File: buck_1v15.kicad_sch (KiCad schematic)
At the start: 21 parts

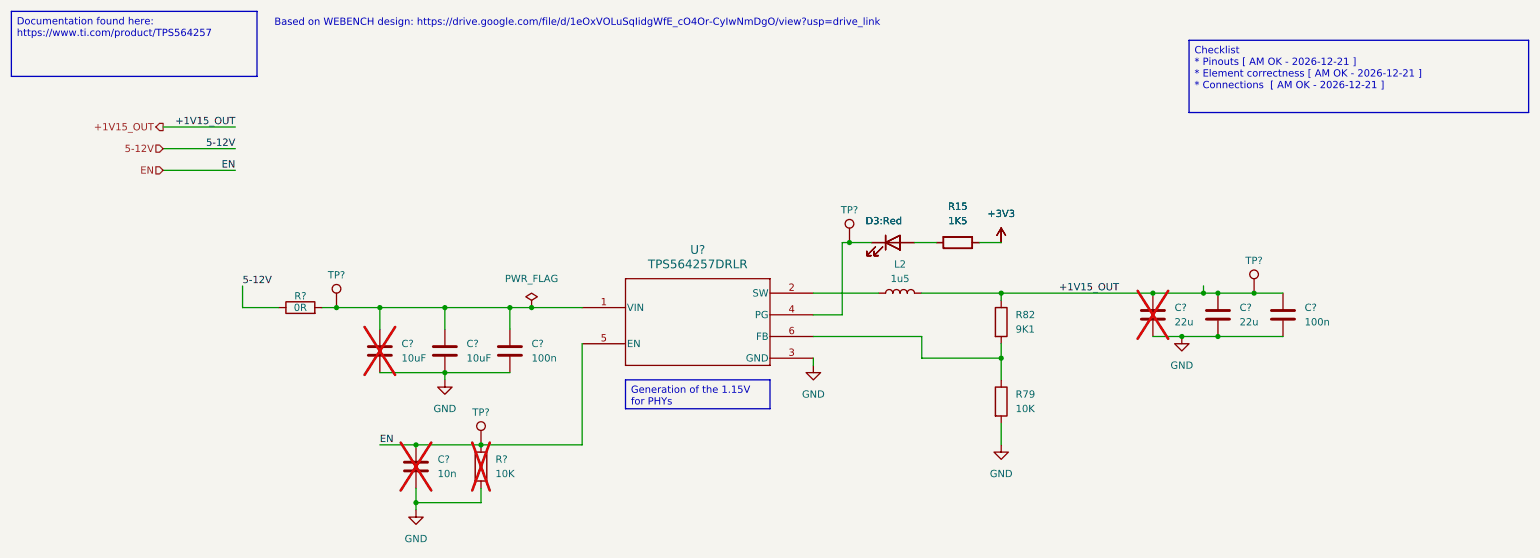
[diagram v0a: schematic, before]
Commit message: towards a merge conflict free schematic. Refs: #9
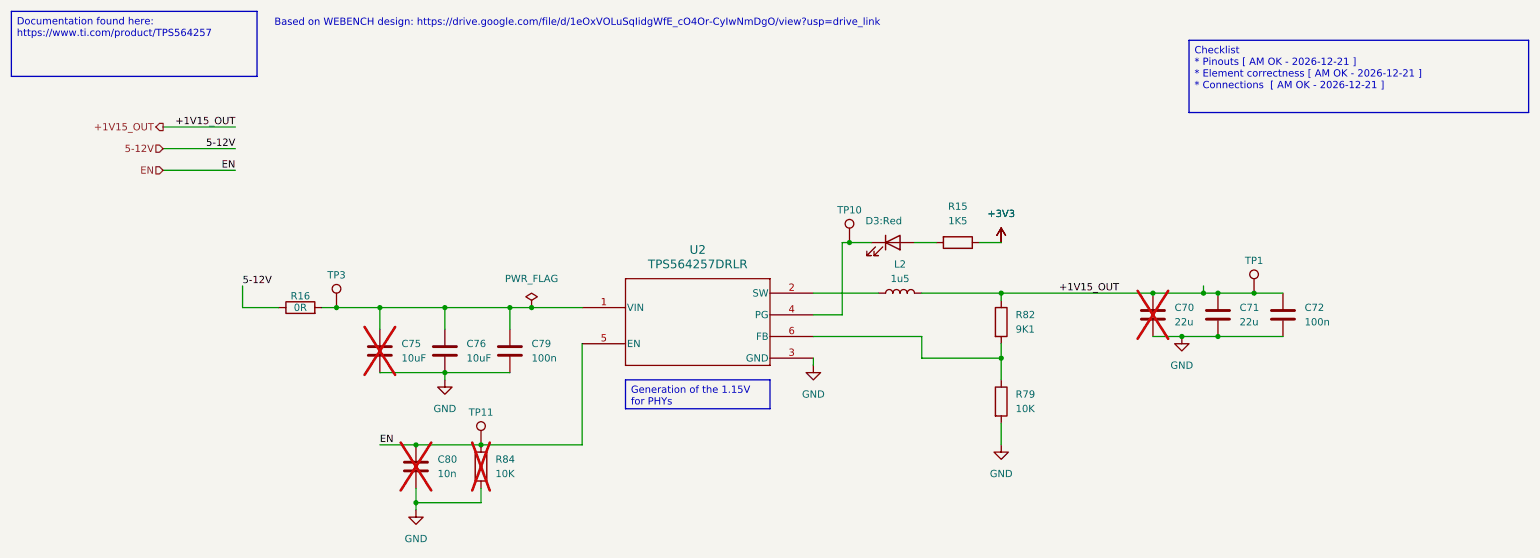
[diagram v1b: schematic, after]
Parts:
- removed D3: LED_{color}_{U_F}_{I_F}, KL_Footprints:LED_0603, symbol KL_LED:LED_red_2V_0.03A
- removed R15: 1K5, KL_Footprints:R_0603, symbol KL_R:R_1K5_100mW_5_0603
- gave numbers to parts that had none: 14

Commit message: open project in KiCAD10. Refs: #41
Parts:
- TP1, TP10, TP11, TP3: value ~ -> (none)

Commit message: updates buck_1v15. Refs: #41
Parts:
- removed C72: 100n, KL_Footprints:C_0603, symbol KL_C:C_100n_10V_X7R_0603_10
- added C72: 100n, KL_Footprints:C_0603, symbol KL_C:C_100n_16V_10pct_X7R_0603
- C70, C71: symbol KL_C:C_22u_10V_X5R_0603_20 -> KL_C:C_22u_10V_20pct_X5R_0603; Dielectric (none) -> X5R; MPN (none) -> GRM187R61A226ME15D; Package_in_inch (none) -> 0603; Tolerance 20 -> (none); Tolerance_in_pct (none) -> 20; Voltage 10V -> (none); Voltage_in_V (none) -> 10
- C75, C76: value 10uF -> 10u; symbol KL_C:C_10u_25V_X5R_0603_20 -> KL_C:C_10u_25V_20pct_X5R_0603; Dielectric (none) -> X5R; MPN (none) -> CL10A106MA8NRNC; Package_in_inch (none) -> 0603; Tolerance 20 -> (none); Tolerance_in_pct (none) -> 20; Voltage 25 -> (none); Voltage_in_V (none) -> 25
- C79: symbol KL_C:C_100n_16V_X7R_0603_10 -> KL_C:C_100n_16V_10pct_X7R_0603; Dielectric (none) -> X7R; MPN (none) -> CC0603KPX7R7BB104; Package_in_inch (none) -> 0603; Tolerance 10 -> (none); Tolerance_in_pct (none) -> 10; Voltage 16V -> (none); Voltage_in_V (none) -> 16
- C80: symbol KL_C:C_10n_50V_X7R_0603_10 -> KL_C:C_10n_50V_10pct_X7R_0603; Dielectric (none) -> X7R; MPN (none) -> CL10B103KB8WPND; Package_in_inch (none) -> 0603; Tolerance 10 -> (none); Tolerance_in_pct (none) -> 10; Voltage 50 -> (none); Voltage_in_V (none) -> 50
- D3: symbol KL_LED:LED_red_2V_0.03A -> KL_LED:LED_Red_2V_0.03A_0603; MPN (none) -> LTST-C194KRKT; Package_in_inch (none) -> 0603
- L2: symbol KL_L:L_1u5_19A_20pct_7L9x7W3 -> KL_L:L_1u5_19A_20pct_7.9x7.3; LCSC C2453564 -> C19947700; MPN (none) -> SRP7050WA-1R5M; Package_LxW_in_mm (none) -> 7.9x7.3; Package_in_inch 0L287X0W287 -> (none); Package_in_mm L7.9XW7.3 -> (none)
- R15: symbol KL_R:R_1K5_100mW_5_0603 -> KL_R:R_1K5_0.1W_5pct_0603; MPN (none) -> AC0603JR-071K5L; Package (in) 0603 -> (none); Package_in_inch (none) -> 0603; Power 0.1 -> (none); Power_in_W (none) -> 0.1; Tolerance 5 -> (none); Tolerance_in_pct (none) -> 5
- R16: symbol KL_R:R_0R_2W_5_2512 -> KL_R:R_0R_2W_5pct_2512; MPN (none) -> CRF2512-J/-000ELF; Mouser 652-CRF2512-J-000ELF -> 652-CRF2512-J-000ELF; Package (in) 2512 -> (none); Package_in_inch (none) -> 2512; Power 2 -> (none); Power_in_W (none) -> 2; Tolerance 5 -> (none); Tolerance_in_pct (none) -> 5
- R79, R84: symbol KL_R:R_10K_100mW_5_0603 -> KL_R:R_10K_0.1W_5pct_0603; MPN (none) -> CRCW060310K0JNEC; Package (in) 0603 -> (none); Package_in_inch (none) -> 0603; Power 100mW -> (none); Power_in_W (none) -> 0.1; Tolerance 5% -> (none); Tolerance_in_pct (none) -> 5
- R82: symbol KL_R:R_9K1_100mW_1pct_0603 -> KL_R:R_9K1_0.1W_1pct_0603; MPN (none) -> RC0603FR-079K1L; Package (in) 0603 -> (none); Package_in_inch (none) -> 0603; Power 100 -> (none); Power_in_W (none) -> 0.1; Tolerance 1 -> (none); Tolerance_in_pct (none) -> 1
- TP1, TP10, TP11, TP3: footprint Connector_PinHeader_2.54mm:PinHeader_1x01_P2.54mm_Vertical -> KL_Footprints:TestPoint; symbol KL_TP:TestPoint -> KL_TestPoint:TestPoint
- U2: MPN (none) -> TPS564257DRLR; VIN_MAX_V (none) -> 17; VIN_MIN_V (none) -> 3
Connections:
- net +1V15_OUT: now also C72.1
- net GND: now also C72.2

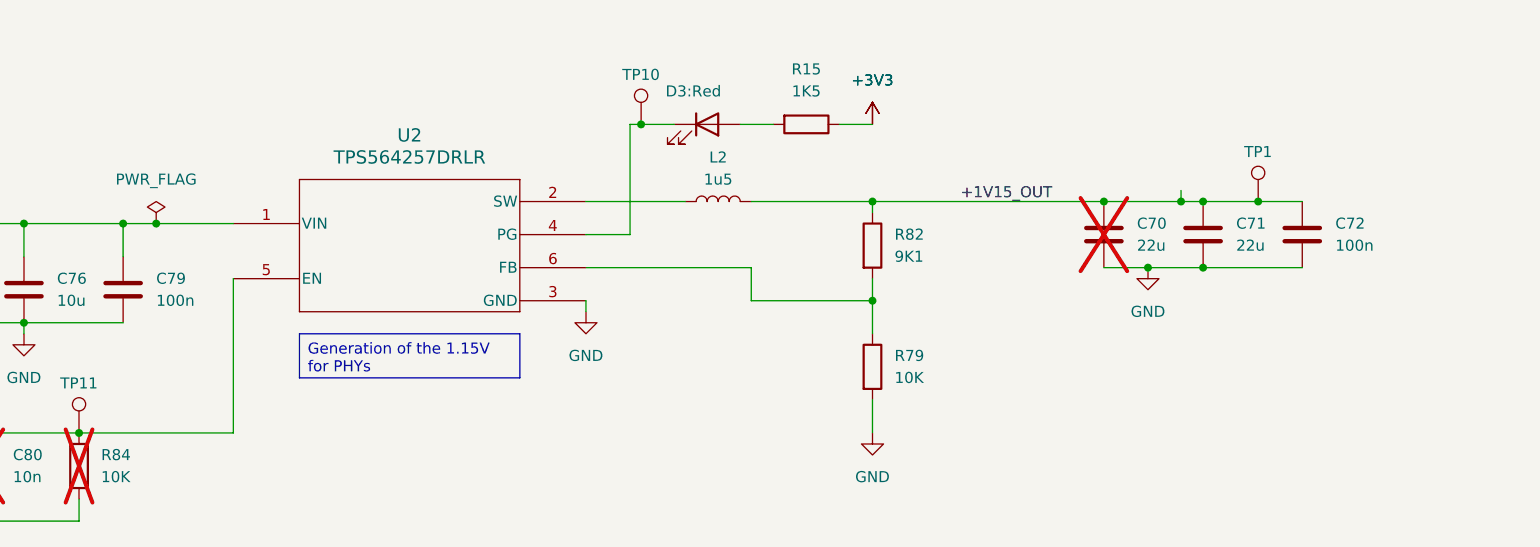
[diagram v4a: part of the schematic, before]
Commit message: replaces all capacitors with 10u. Refs: #52
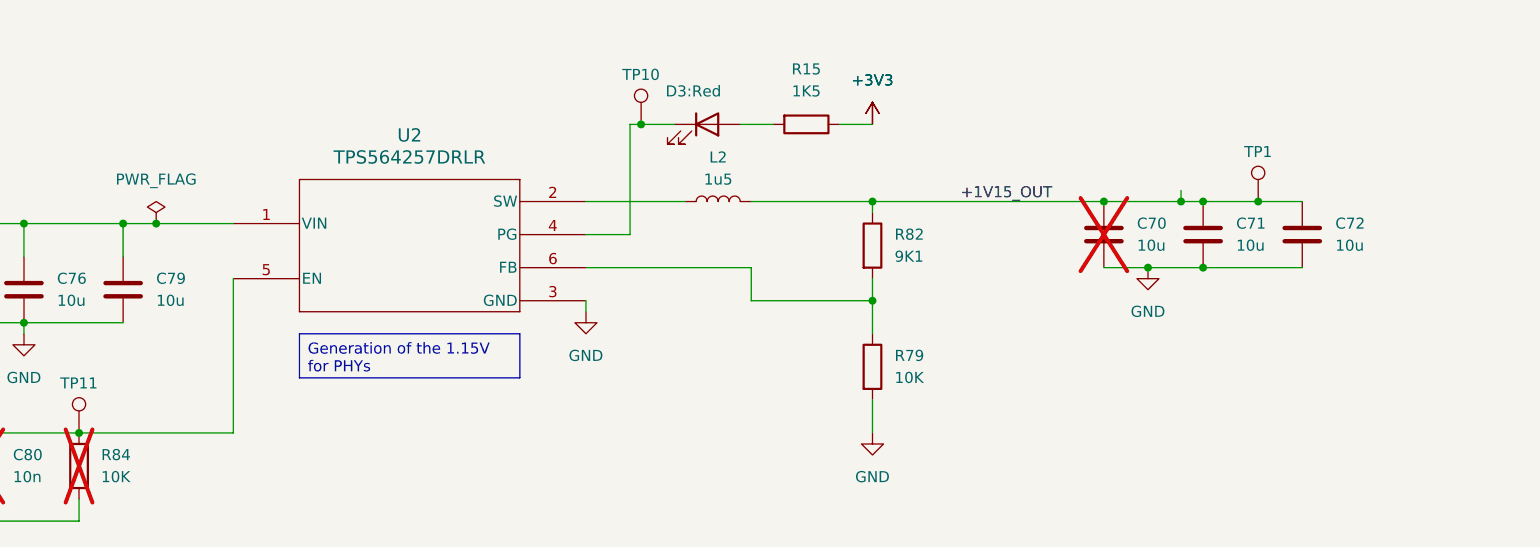
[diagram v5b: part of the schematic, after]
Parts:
- C70, C71: value 22u -> 10u; symbol KL_C:C_22u_10V_20pct_X5R_0603 -> KL_C:C_10u_25V_20pct_X5R_0603; Digikey 490-13243-1-ND -> 1276-1869-1-ND; LCSC C361061 -> C96446; MPN GRM187R61A226ME15D -> CL10A106MA8NRNC; Mouser 81-GRM187R61A226ME5D -> 187-CL10A106MA8NRNC; Voltage_in_V 10 -> 25
- C72, C79: value 100n -> 10u; symbol KL_C:C_100n_16V_10pct_X7R_0603 -> KL_C:C_10u_25V_20pct_X5R_0603; Dielectric X7R -> X5R; Digikey 311-1335-1-ND -> 1276-1869-1-ND; LCSC C2649559 -> C96446; MPN CC0603KPX7R7BB104 -> CL10A106MA8NRNC; Mouser 603-C0603KPX7R7BB104 -> 187-CL10A106MA8NRNC; Tolerance_in_pct 10 -> 20; Voltage_in_V 16 -> 25
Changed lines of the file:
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@@
 	)
 	(symbol
-		(lib_id "KL_C:C_22u_10V_20pct_X5R_0603")
+		(lib_id "KL_C:C_10u_25V_20pct_X5R_0603")
 		(at 226.06 67.31 0)
 		(unit 1)
@@
 			)
 		)
-		(property "Value" "22u"
+		(property "Value" "10u"
 			(at 229.87 68.5799 0)
 			(show_name no)
@@
 			)
 		)
-		(property "Datasheet" "https://pim.murata.com/asset/pim4/ceramicCapacitorSMD/GRM187R61A226ME15-01A-EN_PDF_CERAMICCAPACITORSMD"
+		(property "Datasheet" "https://weblib.samsungsem.com/mlcc/mlcc-ec-data-sheet.do?partNumber=CL10A106MA8NRN"
 			(at 226.06 67.31 0)
 			(hide yes)
@@
 			)
 		)
-		(property "Mouser" "81-GRM187R61A226ME5D"
+		(property "Mouser" "187-CL10A106MA8NRNC"
 			(at 226.06 67.31 0)
 			(hide yes)
@@
 			)
 		)
-		(property "Digikey" "490-13243-1-ND"
+		(property "Digikey" "1276-1869-1-ND"
 			(at 226.06 67.31 0)
 			(hide yes)
@@
 			)
 		)
-		(property "LCSC" "C361061"
+		(property "LCSC" "C96446"
 			(at 226.06 67.31 0)
 			(hide yes)
@@
 			)
 		)
-		(property "Voltage_in_V" "10"
+		(property "Voltage_in_V" "25"
 			(at 226.06 67.31 0)
 			(hide yes)
@@
 			)
 		)
-		(property "MPN" "GRM187R61A226ME15D"
+		(property "MPN" "CL10A106MA8NRNC"
 			(at 226.06 67.31 0)
 			(hide yes)
@@
 	)
 	(symbol
-		(lib_id "KL_C:C_100n_16V_10pct_X7R_0603")
+		(lib_id "KL_C:C_10u_25V_20pct_X5R_0603")
 		(at 101.6 73.66 0)
 		(unit 1)
@@
 			)
 		)
-		(property "Value" "100n"
+		(property "Value" "10u"
 			(at 105.41 74.9299 0)
 			(show_name no)
@@
 			)
 		)
-		(property "Datasheet" "https://yageogroup.com/download/specsheet/CC0603KPX7R7BB104"
+		(property "Datasheet" "https://weblib.samsungsem.com/mlcc/mlcc-ec-data-sheet.do?partNumber=CL10A106MA8NRN"
 			(at 101.6 73.66 0)
 			(hide yes)
@@
 			)
 		)
-		(property "Mouser" "603-C0603KPX7R7BB104"
+		(property "Mouser" "187-CL10A106MA8NRNC"
 			(at 101.6 73.66 0)
 			(hide yes)
@@
 			)
 		)
-		(property "Digikey" "311-1335-1-ND"
+		(property "Digikey" "1276-1869-1-ND"
 			(at 101.6 73.66 0)
 			(hide yes)
@@
 			)
 		)
-		(property "LCSC" "C2649559"
+		(property "LCSC" "C96446"
 			(at 101.6 73.66 0)
 			(hide yes)
@@
 			)
 		)
-		(property "Voltage_in_V" "16"
+		(property "Voltage_in_V" "25"
 			(at 101.6 73.66 0)
 			(hide yes)
@@
 			)
 		)
-		(property "Tolerance_in_pct" "10"
+		(property "Tolerance_in_pct" "20"
 			(at 101.6 73.66 0)
 			(hide yes)
@@
 			)
 		)
-		(property "Dielectric" "X7R"
+		(property "Dielectric" "X5R"
 			(at 101.6 73.66 0)
 			(hide yes)
@@
 			)
 		)
-		(property "MPN" "CC0603KPX7R7BB104"
+		(property "MPN" "CL10A106MA8NRNC"
 			(at 101.6 73.66 0)
 			(hide yes)
@@
 	)
 	(symbol
-		(lib_id "KL_C:C_100n_16V_10pct_X7R_0603")
+		(lib_id "KL_C:C_10u_25V_20pct_X5R_0603")
 		(at 237.49 67.31 0)
 		(unit 1)
@@
 			)
 		)
-		(property "Value" "100n"
+		(property "Value" "10u"
 			(at 241.3 68.5799 0)
 			(show_name no)
@@
 			)
 		)
-		(property "Datasheet" "https://yageogroup.com/download/specsheet/CC0603KPX7R7BB104"
+		(property "Datasheet" "https://weblib.samsungsem.com/mlcc/mlcc-ec-data-sheet.do?partNumber=CL10A106MA8NRN"
 			(at 237.49 67.31 0)
 			(hide yes)
@@
 			)
 		)
-		(property "Mouser" "603-C0603KPX7R7BB104"
+		(property "Mouser" "187-CL10A106MA8NRNC"
 			(at 237.49 67.31 0)
 			(hide yes)
@@
 			)
 		)
-		(property "Digikey" "311-1335-1-ND"
+		(property "Digikey" "1276-1869-1-ND"
 			(at 237.49 67.31 0)
 			(hide yes)
@@
 			)
 		)
-		(property "LCSC" "C2649559"
+		(property "LCSC" "C96446"
 			(at 237.49 67.31 0)
 			(hide yes)
@@
 			)
 		)
-		(property "Voltage_in_V" "16"
+		(property "Voltage_in_V" "25"
 			(at 237.49 67.31 0)
 			(hide yes)
@@
 			)
 		)
-		(property "Tolerance_in_pct" "10"
+		(property "Tolerance_in_pct" "20"
 			(at 237.49 67.31 0)
 			(hide yes)
@@
 			)
 		)
-		(property "Dielectric" "X7R"
+		(property "Dielectric" "X5R"
 			(at 237.49 67.31 0)
 			(hide yes)
@@
 			)
 		)
-		(property "MPN" "CC0603KPX7R7BB104"
+		(property "MPN" "CL10A106MA8NRNC"
 			(at 237.49 67.31 0)
 			(hide yes)
@@
 	)
 	(symbol
-		(lib_id "KL_C:C_22u_10V_20pct_X5R_0603")
+		(lib_id "KL_C:C_10u_25V_20pct_X5R_0603")
 		(at 214.63 67.31 0)
 		(unit 1)
@@
 			)
 		)
-		(property "Value" "22u"
+		(property "Value" "10u"
 			(at 218.44 68.5799 0)
 			(show_name no)
@@
 			)
 		)
-		(property "Datasheet" "https://pim.murata.com/asset/pim4/ceramicCapacitorSMD/GRM187R61A226ME15-01A-EN_PDF_CERAMICCAPACITORSMD"
+		(property "Datasheet" "https://weblib.samsungsem.com/mlcc/mlcc-ec-data-sheet.do?partNumber=CL10A106MA8NRN"
 			(at 214.63 67.31 0)
 			(hide yes)
@@
 			)
 		)
-		(property "Mouser" "81-GRM187R61A226ME5D"
+		(property "Mouser" "187-CL10A106MA8NRNC"
 			(at 214.63 67.31 0)
 			(hide yes)
@@
 			)
 		)
-		(property "Digikey" "490-13243-1-ND"
+		(property "Digikey" "1276-1869-1-ND"
 			(at 214.63 67.31 0)
 			(hide yes)
@@
 			)
 		)
-		(property "LCSC" "C361061"
+		(property "LCSC" "C96446"
 			(at 214.63 67.31 0)
 			(hide yes)
@@
 			)
 		)
-		(property "Voltage_in_V" "10"
+		(property "Voltage_in_V" "25"
 			(at 214.63 67.31 0)
 			(hide yes)
@@
 			)
 		)
-		(property "MPN" "GRM187R61A226ME15D"
+		(property "MPN" "CL10A106MA8NRNC"
 			(at 214.63 67.31 0)
 			(hide yes)
@@
 		)
 	)
-	(embedded_fonts no)
 )
